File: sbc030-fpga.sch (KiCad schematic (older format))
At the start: 0 parts

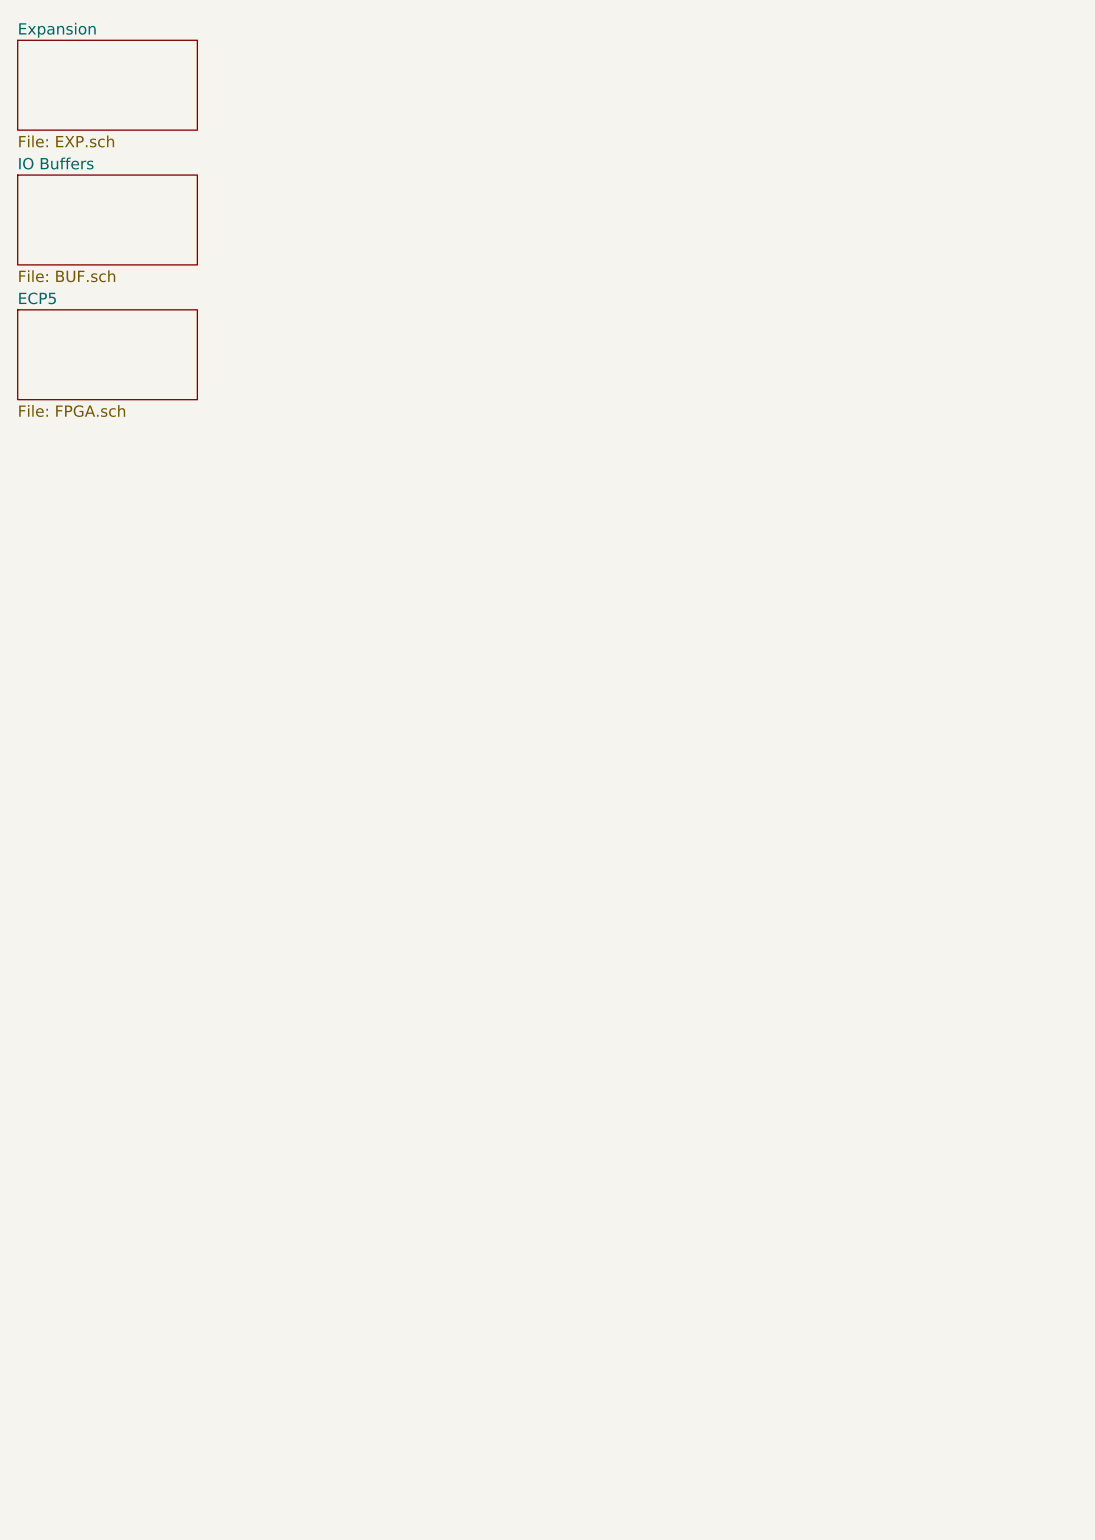
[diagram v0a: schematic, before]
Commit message: updated schematic and initial bga fanout
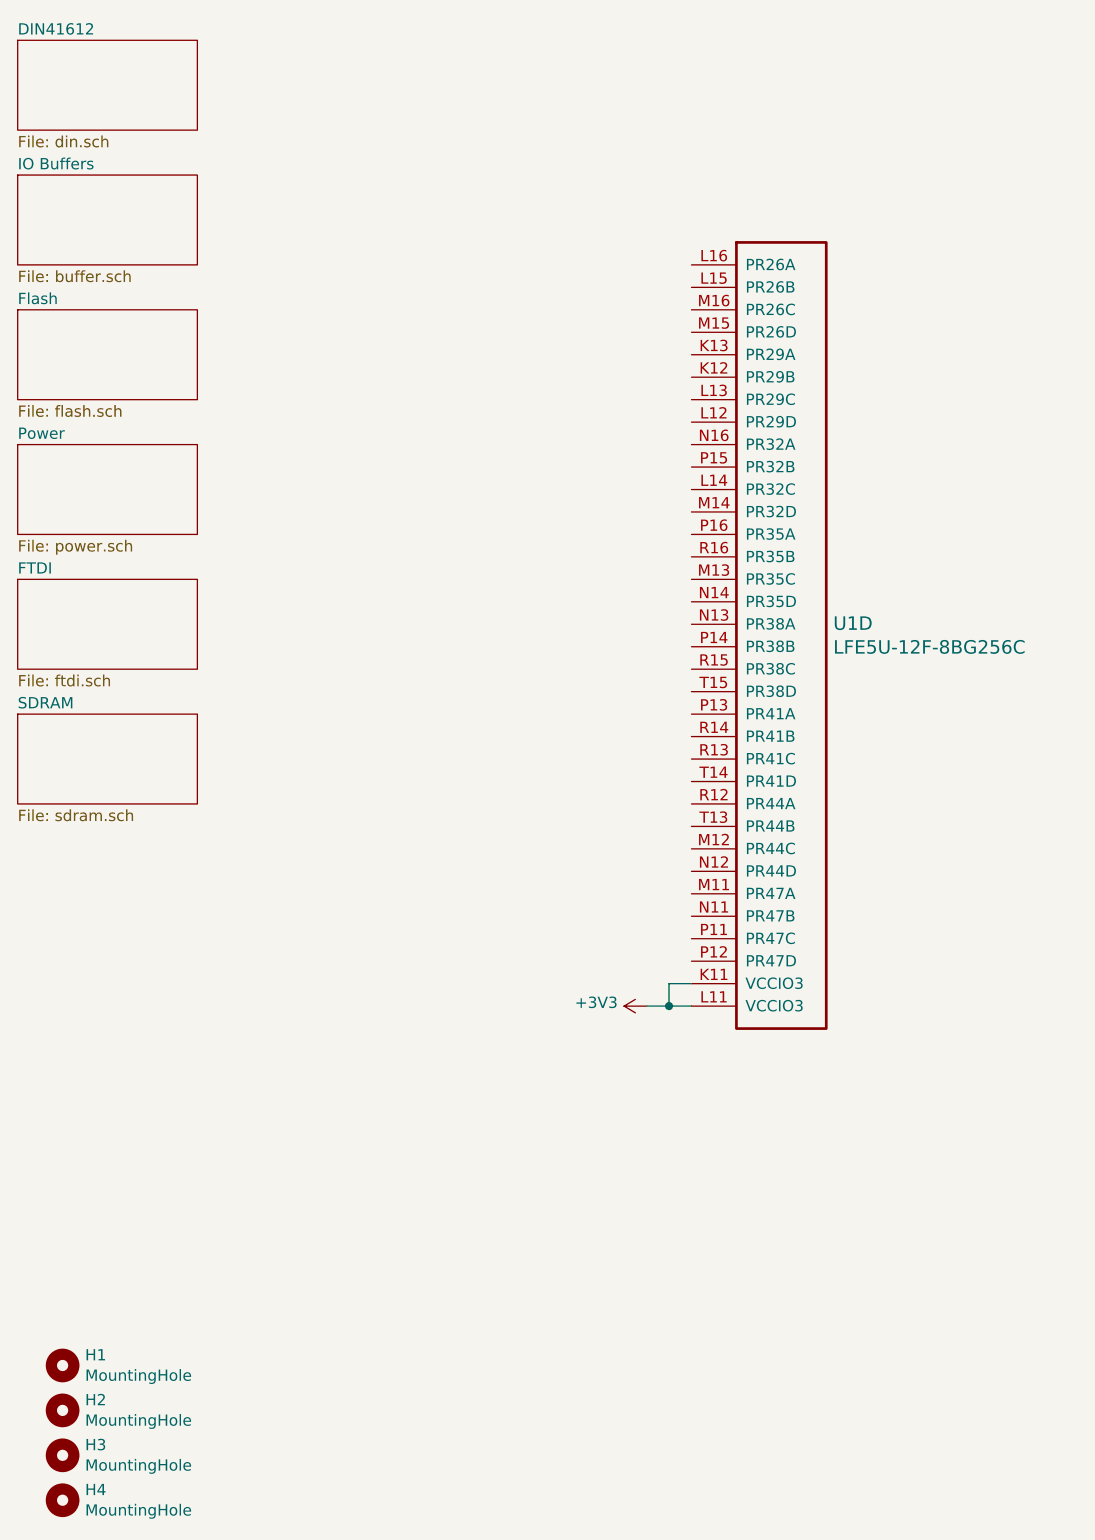
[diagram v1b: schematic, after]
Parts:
- added H1, H2, H3, H4: MountingHole, MountingHole:MountingHole_3.2mm_M3, symbol Mechanical:MountingHole
- added U1: LFE5U-12F-8BG256C, Package_BGA:BGA-256_14.0x14.0mm_Layout16x16_P0.8mm_Ball0.45mm_Pad0.32mm_NSMD, symbol ecp5:LFE5U-12F-8BG256C
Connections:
- new net +3V3: U1.K11 (VCCIO3), U1.L11 (VCCIO3)
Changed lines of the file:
@@
 $Descr A4 11693 8268
 encoding utf-8
-Sheet 1 4
+Sheet 1 7
 Title ""
 Date ""
@@
 S 600  700  800  400
 U 5C254B3E
-F0 "Expansion" 50
-F1 "EXP.sch" 50
+F0 "DIN41612" 50
+F1 "din.sch" 50
 $EndSheet
 $Sheet
@@
 U 5C254FC9
 F0 "IO Buffers" 50
-F1 "BUF.sch" 50
+F1 "buffer.sch" 50
 $EndSheet
 $Sheet
 S 600  1900 800  400
 U 5C254FCC
-F0 "ECP5" 50
-F1 "FPGA.sch" 50
+F0 "Flash" 50
+F1 "flash.sch" 50
 $EndSheet
+$Comp
+L Mechanical:MountingHole H1
+U 1 1 5C2DCF28
+P 800 6600
+F 0 "H1" H 900 6646 50  0000 L CNN
+F 1 "MountingHole" H 900 6555 50  0000 L CNN
+F 2 "MountingHole:MountingHole_3.2mm_M3" H 800 6600 50  0001 C CNN
+F 3 "~" H 800 6600 50  0001 C CNN
+	1    800  6600
+	1    0    0    -1
+$EndComp
+$Comp
+L Mechanical:MountingHole H2
+U 1 1 5C2DCF49
+P 800 6800
+F 0 "H2" H 900 6846 50  0000 L CNN
+F 1 "MountingHole" H 900 6755 50  0000 L CNN
+F 2 "MountingHole:MountingHole_3.2mm_M3" H 800 6800 50  0001 C CNN
+F 3 "~" H 800 6800 50  0001 C CNN
+	1    800  6800
+	1    0    0    -1
+$EndComp
+$Comp
+L Mechanical:MountingHole H3
+U 1 1 5C2DCF69
+P 800 7000
+F 0 "H3" H 900 7046 50  0000 L CNN
+F 1 "MountingHole" H 900 6955 50  0000 L CNN
+F 2 "MountingHole:MountingHole_3.2mm_M3" H 800 7000 50  0001 C CNN
+F 3 "~" H 800 7000 50  0001 C CNN
+	1    800  7000
+	1    0    0    -1
+$EndComp
+$Comp
+L Mechanical:MountingHole H4
+U 1 1 5C2DCF8B
+P 800 7200
+F 0 "H4" H 900 7246 50  0000 L CNN
+F 1 "MountingHole" H 900 7155 50  0000 L CNN
+F 2 "MountingHole:MountingHole_3.2mm_M3" H 800 7200 50  0001 C CNN
+F 3 "~" H 800 7200 50  0001 C CNN
+	1    800  7200
+	1    0    0    -1
+$EndComp
+$Sheet
+S 600  2500 800  400
+U 5C35F269
+F0 "Power" 50
+F1 "power.sch" 50
+$EndSheet
+$Sheet
+S 600  3100 800  400
+U 5C2DEE0B
+F0 "FTDI" 50
+F1 "ftdi.sch" 50
+$EndSheet
+$Sheet
+S 600  3700 800  400
+U 5C2FB052
+F0 "SDRAM" 50
+F1 "sdram.sch" 50
+$EndSheet
+Wire Wire Line
+	3600 4900 3500 4900
+Wire Wire Line
+	3500 4900 3500 5000
+Wire Wire Line
+	3600 5000 3500 5000
+$Comp
+L ecp5:LFE5U-12F-8BG256C U?
+U 4 1 5C30AFAB
+P 3600 1700
+AR Path="/5C254FCC/5C30AFAB" Ref="U?"  Part="4"
+AR Path="/5C35F270/5C30AFAB" Ref="U?"  Part="4"
+AR Path="/5C30AFAB" Ref="U1"  Part="4"
+F 0 "U1" H 4231 103 60  0000 L CNN
+F 1 "LFE5U-12F-8BG256C" H 4231 -3  60  0000 L CNN
+F 2 "Package_BGA:BGA-256_14.0x14.0mm_Layout16x16_P0.8mm_Ball0.45mm_Pad0.32mm_NSMD" H 3800 1750 60  0001 L CNN
+F 3 "" H 3600 1700 50  0001 C CNN
+	4    3600 1700
+	1    0    0    -1
+$EndComp
+Wire Wire Line
+	3400 5000 3500 5000
+Connection ~ 3500 5000
+$Comp
+L power:+3V3 #PWR?
+U 1 1 5C30AFD2
+P 3400 5000
+AR Path="/5C35F270/5C30AFD2" Ref="#PWR?"  Part="1"
+AR Path="/5C30AFD2" Ref="#PWR0152"  Part="1"
+F 0 "#PWR0152" H 3400 4850 50  0001 C CNN
+F 1 "+3V3" V 3415 5128 50  0000 L CNN
+F 2 "" H 3400 5000 50  0001 C CNN
+F 3 "" H 3400 5000 50  0001 C CNN
+	1    3400 5000
+	0    -1   -1   0
+$EndComp
 $EndSCHEMATC

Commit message: add hdmi output
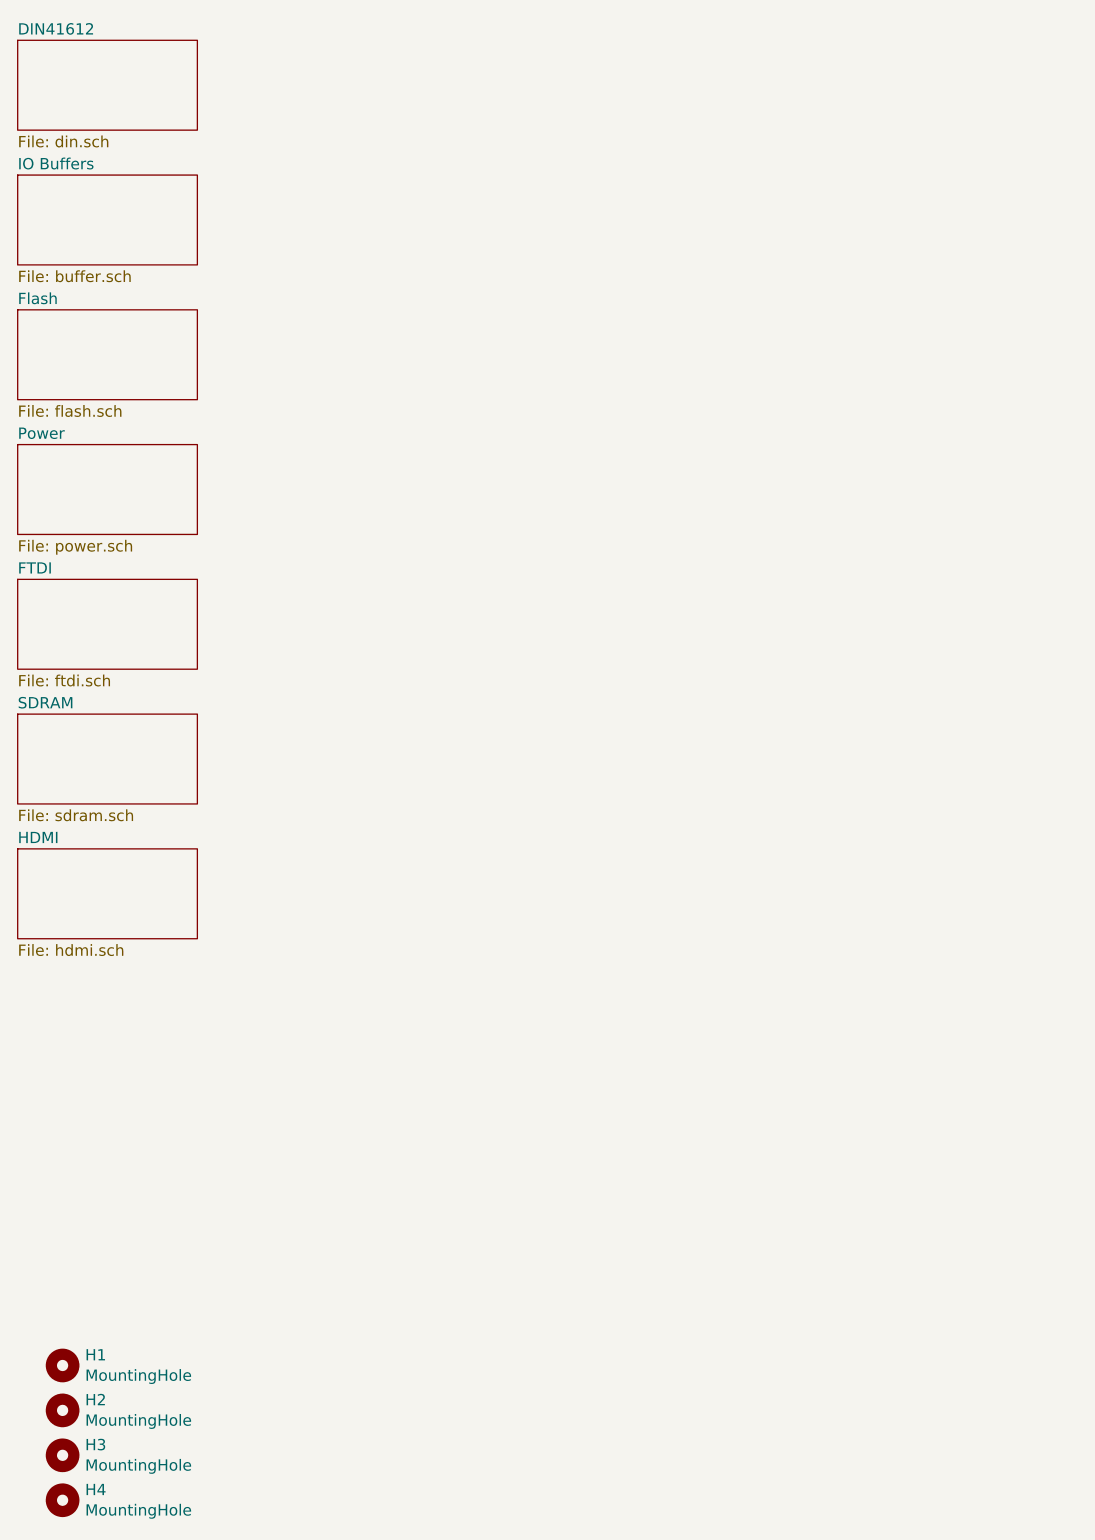
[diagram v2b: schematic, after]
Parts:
- removed U1: LFE5U-12F-8BG256C, Package_BGA:BGA-256_14.0x14.0mm_Layout16x16_P0.8mm_Ball0.45mm_Pad0.32mm_NSMD, symbol ecp5:LFE5U-12F-8BG256C
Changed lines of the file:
@@
 $Descr A4 11693 8268
 encoding utf-8
-Sheet 1 7
+Sheet 1 8
 Title ""
 Date ""
@@
 F1 "sdram.sch" 50
 $EndSheet
-Wire Wire Line
-	3600 4900 3500 4900
-Wire Wire Line
-	3500 4900 3500 5000
-Wire Wire Line
-	3600 5000 3500 5000
-$Comp
-L ecp5:LFE5U-12F-8BG256C U?
-U 4 1 5C30AFAB
-P 3600 1700
-AR Path="/5C254FCC/5C30AFAB" Ref="U?"  Part="4"
-AR Path="/5C35F270/5C30AFAB" Ref="U?"  Part="4"
-AR Path="/5C30AFAB" Ref="U1"  Part="4"
-F 0 "U1" H 4231 103 60  0000 L CNN
-F 1 "LFE5U-12F-8BG256C" H 4231 -3  60  0000 L CNN
-F 2 "Package_BGA:BGA-256_14.0x14.0mm_Layout16x16_P0.8mm_Ball0.45mm_Pad0.32mm_NSMD" H 3800 1750 60  0001 L CNN
-F 3 "" H 3600 1700 50  0001 C CNN
-	4    3600 1700
-	1    0    0    -1
-$EndComp
-Wire Wire Line
-	3400 5000 3500 5000
-Connection ~ 3500 5000
-$Comp
-L power:+3V3 #PWR?
-U 1 1 5C30AFD2
-P 3400 5000
-AR Path="/5C35F270/5C30AFD2" Ref="#PWR?"  Part="1"
-AR Path="/5C30AFD2" Ref="#PWR0152"  Part="1"
-F 0 "#PWR0152" H 3400 4850 50  0001 C CNN
-F 1 "+3V3" V 3415 5128 50  0000 L CNN
-F 2 "" H 3400 5000 50  0001 C CNN
-F 3 "" H 3400 5000 50  0001 C CNN
-	1    3400 5000
-	0    -1   -1   0
-$EndComp
+$Sheet
+S 600  4300 800  400
+U 5C3669B9
+F0 "HDMI" 50
+F1 "hdmi.sch" 50
+$EndSheet
 $EndSCHEMATC
